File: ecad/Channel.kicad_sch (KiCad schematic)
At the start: 20 parts, among them J5 Amphenol_10061913-xx0, U15 NE5532, U16 NE5532, U17 TLP4026G, U18 TLP4026G, U8 NE5532

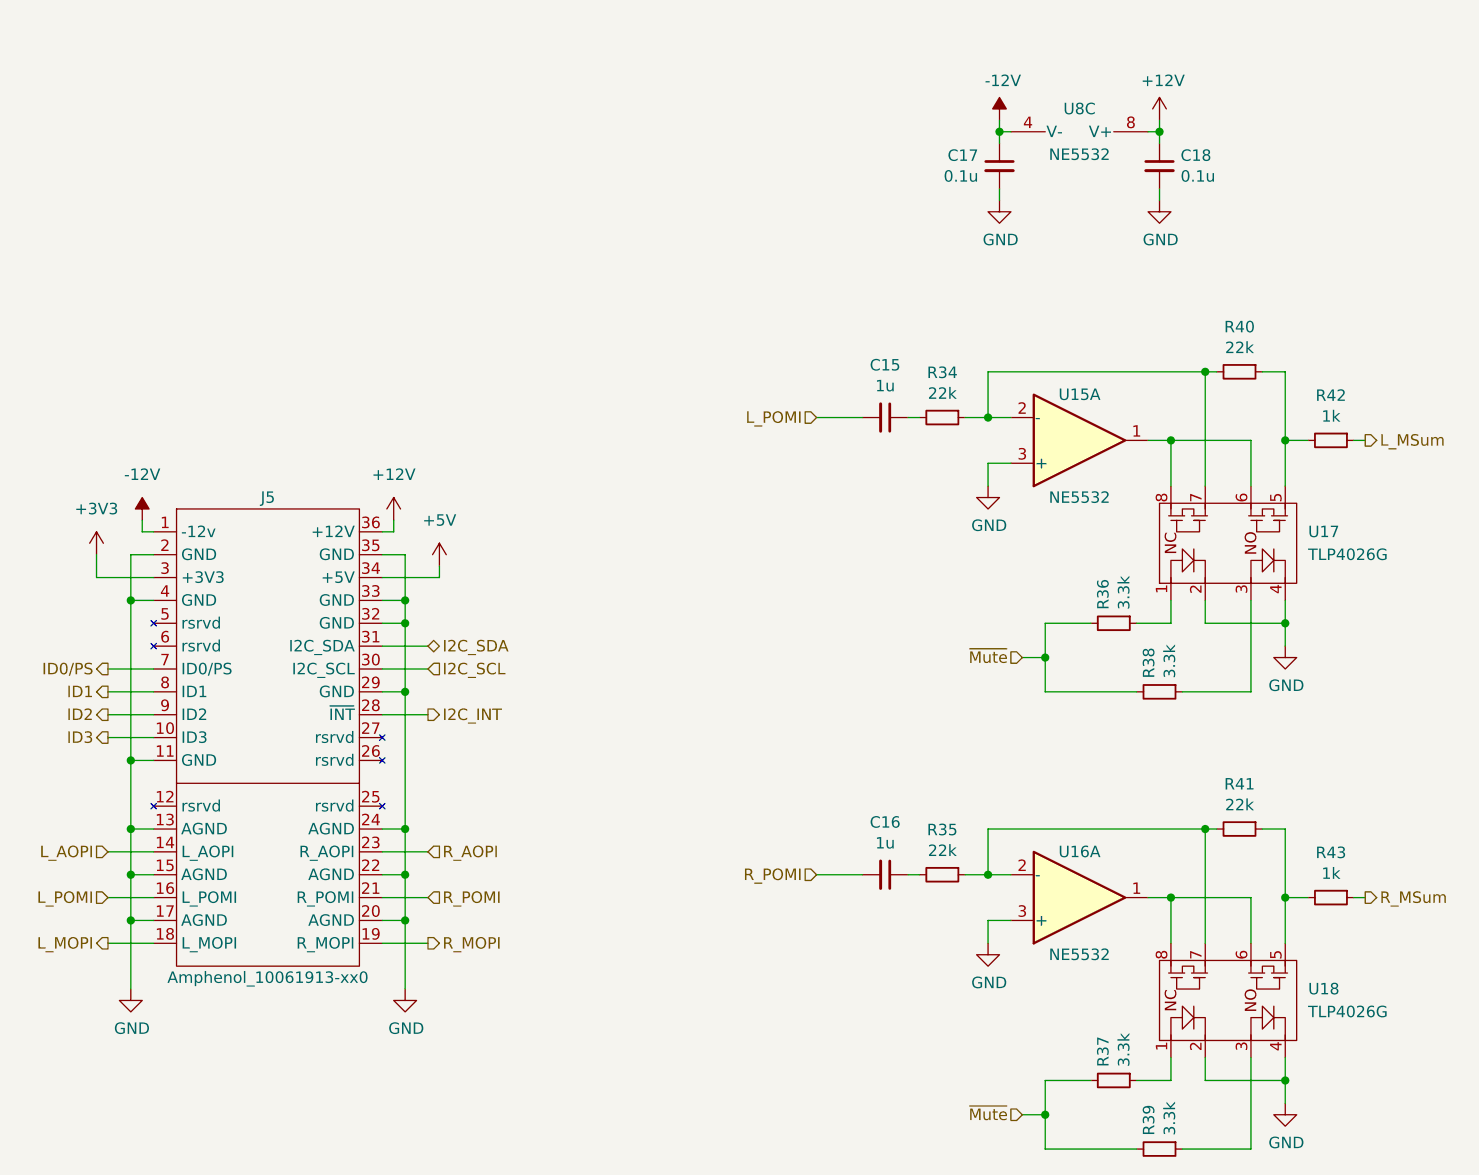
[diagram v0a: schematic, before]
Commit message: Update to Kicad 7 and generate PDF schematic.
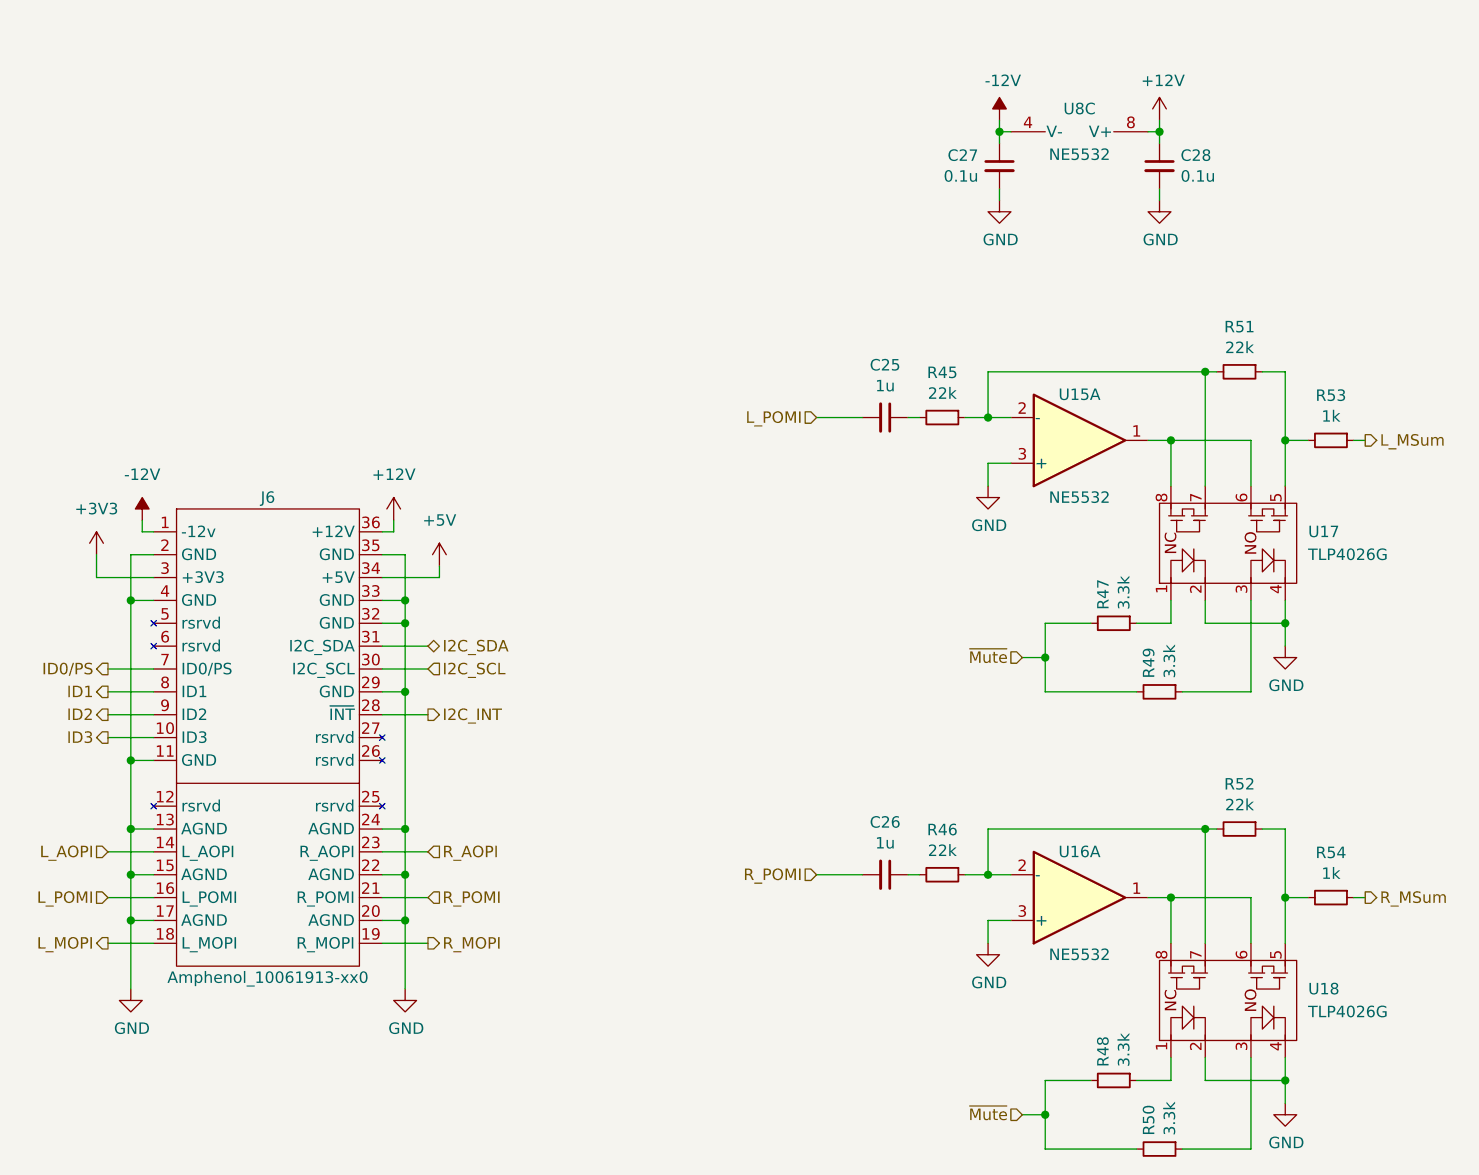
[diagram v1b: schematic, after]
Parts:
- renumbered C15 to C25, C16 to C26, C17 to C27, C18 to C28, J5 to J6, R34 to R45, R35 to R46, R36 to R47, R37 to R48, R38 to R49, R39 to R50, R40 to R51, R41 to R52, R42 to R53, R43 to R54

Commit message: Fixes to footprint numbering in multi-unit parts.
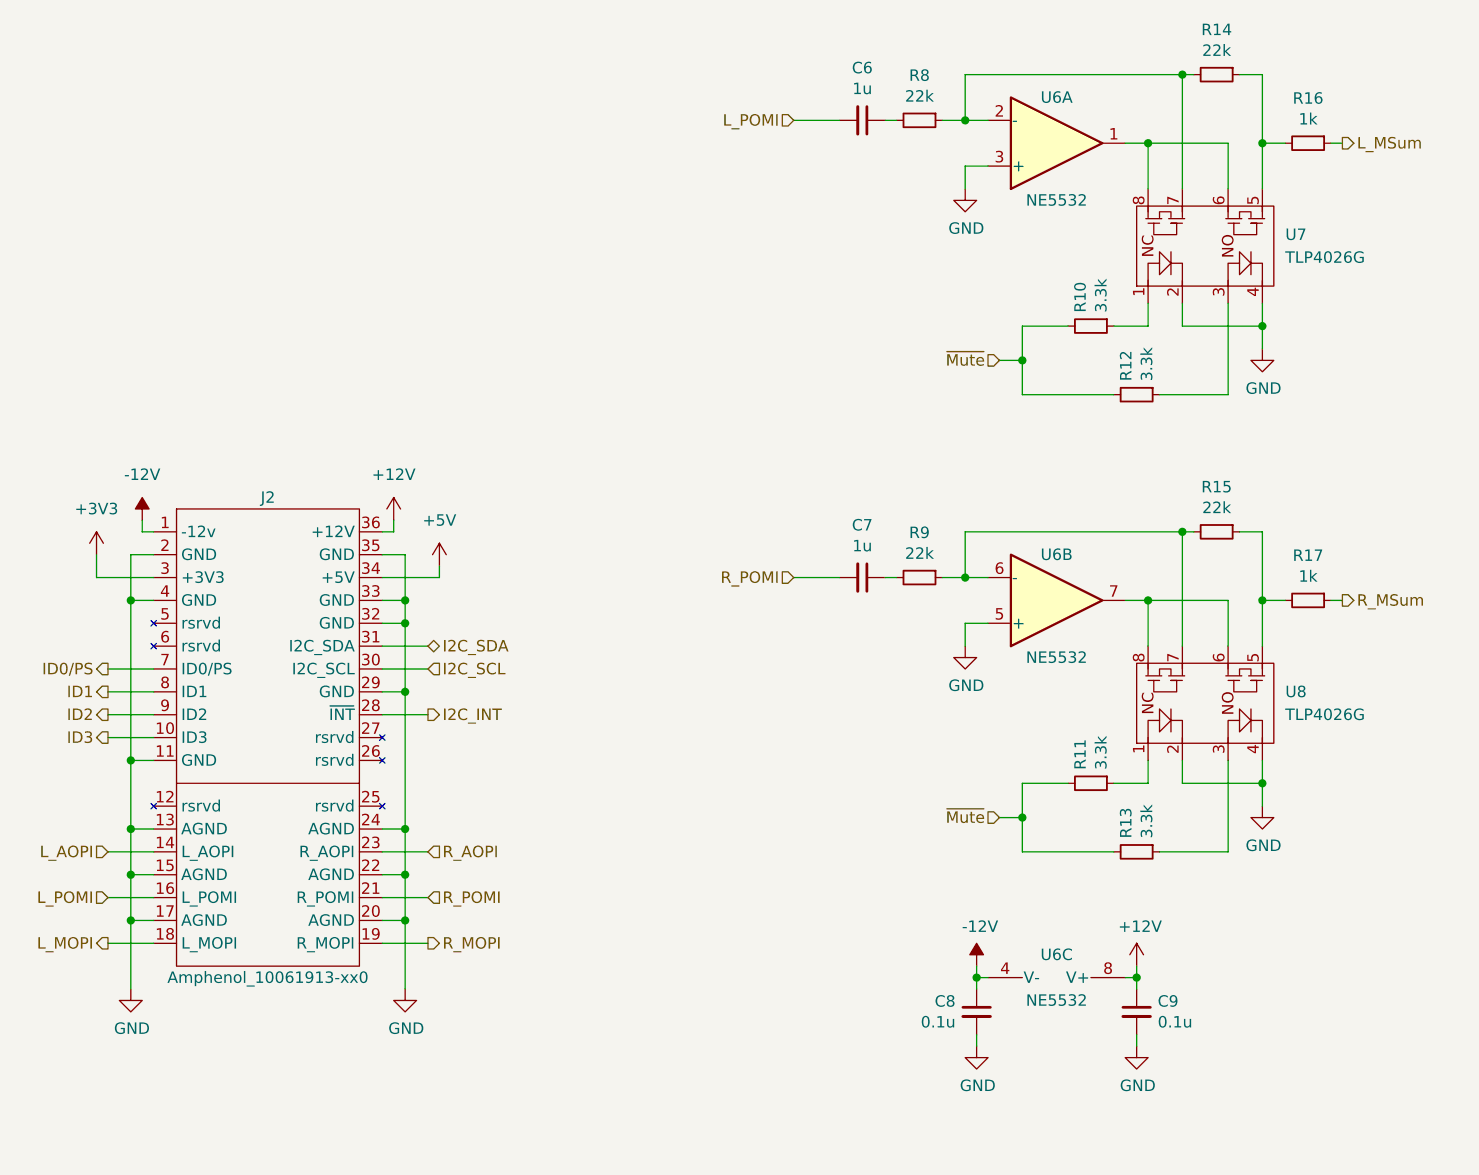
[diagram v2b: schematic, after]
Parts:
- renumbered C25 to C6, C26 to C7, C27 to C8, C28 to C9, J6 to J2, R47 to R10, R48 to R11, R49 to R12, R50 to R13, R51 to R14, R52 to R15, R53 to R16, R54 to R17, R45 to R8, R46 to R9, U15 to U6, U8 to U6, U16 to U6, U17 to U7, U18 to U8
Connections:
- net GND: now also U6.5 (+); no longer U6.3 (+)
- net at U8.6, U8.8: now also U6.7; no longer U6.1
- net at R15.2, R9.1, U8.7: now also U6.6 (-); no longer U6.2 (-)
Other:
- moved on the sheet: C6, C7, C8, C9, R10, R11, R12, R13, R14, R15, R16, R17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
